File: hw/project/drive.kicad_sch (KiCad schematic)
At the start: 45 parts, among them Q3 STL110N10F7, Q4 STL110N10F7, Q5 STL110N10F7, Q6 STL110N10F7, Q7 STL110N10F7, Q8 STL110N10F7

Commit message: Update sheet settings
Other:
- company: (none) -> Electrium Mobility
- title: (none) -> ESC 2026 - Drive
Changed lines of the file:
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@@
 	(generator_version "10.0")
 	(paper "A4")
+	(title_block
+		(title "ESC 2026 - Drive")
+		(date "2026-06-30")
+		(rev "v2")
+		(company "Electrium Mobility")
+		(comment 1 "Author: Leopoldo Mendoza")
+	)
 	(rectangle
 		(start 93.98 110.49)

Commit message: Continue phase voltage circuit tom
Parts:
- added R52: R_US, Resistor_SMD:R_0805_2012Metric_Pad1.20x1.40mm_HandSolder, symbol Device:R_US
- added R70: R_US, symbol Device:R_US
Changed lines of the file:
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@@
 		)
 	)
+	(text_box "Phase Voltage Sense\n\nExpecting 60Vmax, so R1=47k (0805), R2=2.49k (0603), Cf=2.2nF (>=16V)\n\nNote: Phase Voltage =/= BEMF\n\nBoth FOC and 6-step require the phase voltages to be measured to determine BEMF, thus they require the same circuitry for measuring the phase voltages\n\n6-step\n- With 6-step, zero-crossings are detected EITHER in-software (by sampling the voltage directly with ADC) OR in-hardware (by using a comparator to detect the crossing)\n- This board will only support SOFTWARE-based zero-crossing detection, so the associated pins only require ADCx and not COMPx\n- Note: Virtual Neutral Point could also be determined in either SW or HW, but choosing SW (see Control sheet)"
+		(exclude_from_sim no)
+		(at 78.74 155.194 0)
+		(size 86.36 36.6624)
+		(margins 0.9525 0.9525 0.9525 0.9525)
+		(stroke
+			(width 0)
+			(type solid)
+		)
+		(fill
+			(type none)
+		)
+		(effects
+			(font
+				(size 1.27 1.27)
+			)
+			(justify left top)
+		)
+	)
 	(text_box "PGA Configuration: Inverting Mode (non-inverting disallows DC bias) (AN5306 3.4.1)\n\nVINP (OPP/non-inverting)\n- HW: NC, free up pins with OPAMPx_VINP for other periphs\n- FW: VP_SEL[1:0] = 11 to cut off VINP and route internal DAC ch (RM0440 25.3.4)\n\nVINM (OPN/inverting)\n- HW: small R to limit curr (R1_internal=10k => G_error=0.1%)\n- FW: VM_SEL[1:0] = 10 to enable PGA mode (internal feedback R's) (AN5306 3.4.1)\n\nVOUT (OPO)\n- HW: NC, free up pins with OPAMPx_VOUT for other periphs\n- FW: OPAINTOEN = 1 to cut off VOUT and route internal ADC ch (RM0440 25.3.4)\n\nPGA_GAIN[4:0] = 8 to 13 to implement an inverting amplifier (12=>-31, 13=>-63)"
 		(exclude_from_sim no)
@@
 		)
 	)
+	(label "W"
+		(at 195.58 62.23 0)
+		(effects
+			(font
+				(size 1.27 1.27)
+			)
+			(justify left bottom)
+		)
+	)
 	(label "VSHUNT_U+"
 		(at 38.1 88.9 0)
@@
 		)
 	)
+	(label "U"
+		(at 58.42 60.96 0)
+		(effects
+			(font
+				(size 1.27 1.27)
+			)
+			(justify left bottom)
+		)
+	)
 	(label "VSHUNT_W-"
 		(at 200.66 95.25 0)
@@
 		)
 	)
+	(label "V"
+		(at 127 62.23 0)
+		(effects
+			(font
+				(size 1.27 1.27)
+			)
+			(justify left bottom)
+		)
+	)
 	(label "VSHUNT_V+"
 		(at 92.71 123.19 180)
@@
 		)
 	)
+	(label "U"
+		(at 21.59 158.75 180)
+		(effects
+			(font
+				(size 1.27 1.27)
+			)
+			(justify right bottom)
+		)
+	)
 	(label "VSHUNT_U-"
 		(at 63.5 93.98 0)
@@
 		)
 	)
+	(hierarchical_label "VPHASE_U"
+		(shape output)
+		(at 49.53 157.48 0)
+		(effects
+			(font
+				(size 1.27 1.27)
+			)
+			(justify left)
+		)
+	)
 	(hierarchical_label "GLS3"
 		(shape input)
@@
 	)
 	(symbol
+		(lib_id "Device:R_US")
+		(at 31.75 168.91 180)
+		(unit 1)
+		(body_style 1)
+		(exclude_from_sim no)
+		(in_bom yes)
+		(on_board yes)
+		(in_pos_files yes)
+		(dnp no)
+		(fields_autoplaced yes)
+		(property "Reference" "R70"
+			(at 34.29 167.6399 0)
+			(show_name no)
+			(do_not_autoplace no)
+			(effects
+				(font
+					(size 1.27 1.27)
+				)
+				(justify right)
+			)
+		)
+		(property "Value" "R_US"
+			(at 34.29 170.1799 0)
+			(show_name no)
+			(do_not_autoplace no)
+			(effects
+				(font
+					(size 1.27 1.27)
+				)
+				(justify right)
+			)
+		)
+		(property "Footprint" ""
+			(at 30.734 168.656 90)
+			(hide yes)
+			(show_name no)
+			(do_not_autoplace no)
+			(effects
+				(font
+					(size 1.27 1.27)
+				)
+			)
+		)
+		(property "Datasheet" ""
+			(at 31.75 168.91 0)
+			(hide yes)
+			(show_name no)
+			(do_not_autoplace no)
+			(effects
+				(font
+					(size 1.27 1.27)
+				)
+			)
+		)
+		(property "Description" "Resistor, US symbol"
+			(at 31.75 168.91 0)
+			(hide yes)
+			(show_name no)
+			(do_not_autoplace no)
+			(effects
+				(font
+					(size 1.27 1.27)
+				)
+			)
+		)
+		(pin "1"
+		)
+		(pin "2"
+		)
+		(instances
+			(project "esc"
+				(path "/86a17c4d-db96-42a1-af84-d43fe593f4e6/f702d253-729e-40c3-ac6b-420be83d0138"
+					(reference "R70")
+					(unit 1)
+				)
+			)
+		)
+	)
+	(symbol
 		(lib_id "Device:R_Shunt_US")
 		(at 101.6 92.71 0)
@@
 					(unit 1)
 				)
+			)
+		)
+	)
+	(symbol
+		(lib_id "Device:R_US")
+		(at 31.75 158.75 180)
+		(unit 1)
+		(body_style 1)
+		(exclude_from_sim no)
+		(in_bom yes)
+		(on_board yes)
+		(in_pos_files yes)
+		(dnp no)
+		(fields_autoplaced yes)
+		(property "Reference" "R52"
+			(at 34.29 157.4799 0)
+			(show_name no)
+			(do_not_autoplace no)
+			(effects
+				(font
+					(size 1.27 1.27)
+				)
+				(justify right)
+			)
+		)
+		(property "Value" "R_US"
+			(at 34.29 160.0199 0)
+			(show_name no)
+			(do_not_autoplace no)
+			(effects
+				(font
+					(size 1.27 1.27)
+				)
+				(justify right)
+			)
+		)
+		(property "Footprint" "Resistor_SMD:R_0805_2012Metric_Pad1.20x1.40mm_HandSolder"
+			(at 30.734 158.496 90)
+			(hide yes)
+			(show_name no)
+			(do_not_autoplace no)
+			(effects
+				(font
+					(size 1.27 1.27)
+				)
+			)
+		)
+		(property "Datasheet" ""
+			(at 31.75 158.75 0)
+			(hide yes)
+			(show_name no)
+			(do_not_autoplace no)
+			(effects
+				(font
+					(size 1.27 1.27)
+				)
+			)
+		)
+		(property "Description" "Resistor, US symbol"
+			(at 31.75 158.75 0)
+			(hide yes)
+			(show_name no)
+			(do_not_autoplace no)
+			(effects
+				(font
+					(size 1.27 1.27)
+				)
+			)
+		)
+		(pin "1"
+		)
+		(pin "2"
+		)
+		(instances
+			(project "esc"
+				(path "/86a17c4d-db96-42a1-af84-d43fe593f4e6/f702d253-729e-40c3-ac6b-420be83d0138"
+					(reference "R52")
+					(unit 1)
+				)

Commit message: Add phase voltage first draft
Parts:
- added C23, C52, C54: 470pF/50V, symbol Device:C
- added R72, R76, R79: 2.2k, Resistor_SMD:R_0603_1608Metric_Pad0.98x0.95mm_HandSolder, symbol Device:R_US
- added R74, R75, R77, R78: 22k, Resistor_SMD:R_0603_1608Metric_Pad0.98x0.95mm_HandSolder, symbol Device:R_US
- R52: value R_US -> 22k; footprint Resistor_SMD:R_0805_2012Metric_Pad1.20x1.40mm_HandSolder -> Resistor_SMD:R_0603_1608Metric_Pad0.98x0.95mm_HandSolder
- R70: value R_US -> 22k; footprint (none) -> Resistor_SMD:R_0603_1608Metric_Pad0.98x0.95mm_HandSolder
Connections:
- net GND: now also C23.2, C52.2, C54.2, R72.1, R76.1, R79.1
- net U: now also R70.1
- net V: now also R74.1
- net VPHASE_U: now also R52.2, C23.1, R72.2
- net W: now also R77.1
- net at R70.2: now also R52.1
- new net: R77.2, R78.1
- new net: R74.2, R75.1
- new net VPHASE_V: C52.1, R75.2, R76.2
- new net VPHASE_W: C54.1, R78.2, R79.2
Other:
- note added: "R2/(R1+R2) = 1/21 = 0.04762 {60} [V] -> {2.857} [V]"
- note added: "R_eq = R1 || R2 = 2.1k, C_f = 470 pF => tau = 0.985 us, f_c = 161.6 kHz"
- note added: "Voltage Sense U"
- note added: "Voltage Sense V"
- note added: "Voltage Sense W"
- note added: "add schottkys?"
- note added: "footprint for C_f: C0G (NP0)/5%"
- moved on the sheet: C35, C36, C37, C38, C39, C40, D4, D5, D6, D7, Q5, Q6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

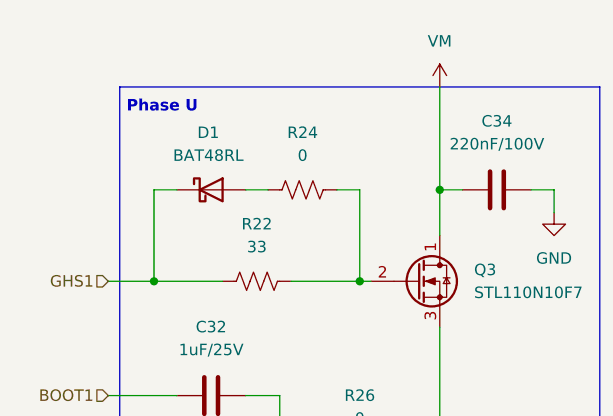
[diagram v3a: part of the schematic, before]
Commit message: Finalize VCC regulator and VDD sections
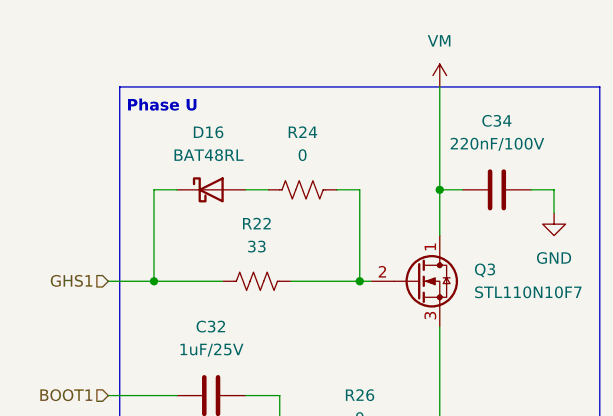
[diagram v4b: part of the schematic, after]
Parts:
- renumbered D1 to D16
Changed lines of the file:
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@@
 		(dnp no)
 		(fields_autoplaced yes)
-		(property "Reference" "D1"
+		(property "Reference" "D16"
 			(at 32.7025 25.4 0)
 			(show_name no)
@@
 			(project "esc"
 				(path "/86a17c4d-db96-42a1-af84-d43fe593f4e6/f702d253-729e-40c3-ac6b-420be83d0138"
-					(reference "D1")
+					(reference "D16")
 					(unit 1)
 				)

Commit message: Finalize phase voltage sensing
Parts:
- removed C33: DNP, symbol Device:C
- removed C39: DNP, Capacitor_SMD:C_0603_1608Metric, symbol Device:C_Small
- removed C52, C54: 470pF/50V, symbol Device:C
- removed R52, R70, R74, R75, R77, R78: 22k, Resistor_SMD:R_0603_1608Metric_Pad0.98x0.95mm_HandSolder, symbol Device:R_US
- removed R76, R79: 2.2k, Resistor_SMD:R_0603_1608Metric_Pad0.98x0.95mm_HandSolder, symbol Device:R_US
- added C33: 470pF/50V, Capacitor_SMD:C_0603_1608Metric, symbol Device:C_Small
- added C57, C58, C59: 1nF, Capacitor_SMD:C_0603_1608Metric, symbol Device:C_Small
- added D35, D36, D37, D38, D39, D40: BAT30K, Diode_SMD:D_SOD-523, symbol Device:D_Schottky
- added R52, R7, R70, R74, R76, R77: 22k, Resistor_SMD:R_0603_1608Metric, symbol Device:R_Small_US
- added R75, R78: 2.2k, Resistor_SMD:R_0603_1608Metric, symbol Device:R_Small_US
- C23: footprint (none) -> Capacitor_SMD:C_0603_1608Metric; symbol Device:C -> Device:C_Small
- C32, C34: symbol Device:C -> Device:C_Small
- C36: value DNP -> 470pF/50V
- R21, R22, R23, R24, R25, R26: symbol Device:R_US -> Device:R_Small_US
- R72: footprint Resistor_SMD:R_0603_1608Metric_Pad0.98x0.95mm_HandSolder -> Resistor_SMD:R_0603_1608Metric; symbol Device:R_US -> Device:R_Small_US
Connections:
- net BOOT1: no longer C32.1
- net GHS1: no longer R22.1
- net GLS1: no longer R23.1
- net GND: now also C33.2, C57.1, C58.1, C59.1, D36.2 (A), D38.2 (A), D40.2 (A), R75.1, R78.1; no longer C34.2
- net OPN_U: now also C57.2; no longer R21.2
- net OPN_V: now also C58.2; no longer C36.1
- net OPN_W: now also C59.2
- net OUT1: no longer C32.2, R26.1
- net U: now also R7.1; no longer R26.2
- net V: now also R70.1
- net VM: no longer C34.1
- net VPHASE_U: now also D35.2 (A), D36.1 (K), R52.2
- net VPHASE_V: now also C33.1, D37.2 (A), D38.1 (K), R74.2, R75.2
- net VPHASE_W: now also C36.1, D39.2 (A), D40.1 (K), R77.2, R78.2
- net VSHUNT_U+: no longer R21.1
- net W: now also R76.1
- net at D3.2 (A): no longer R25.1
- net at R24.1: no longer D16.2 (A)
- new net: R76.2, R77.1
- new net: R70.2, R74.1
- new net: R52.1, R7.2
- new net VDD: D35.1 (K), D37.1 (K), D39.1 (K)
- now unconnected: Q3.2 (G), Q4.2 (G), R22.2, R23.2, R24.2, R25.2
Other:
- note added: "Layout Note: Low-Impedance Power-to-Analog Ground Planes: Ensure your PCB layout uses a continuous, low-impedance ground plane underneath the SoC and power stage. Keep the distance between the low-side shunt ground return and the STSPIN32G4 ground pins as short and wide as possible to minimize $I \times R$ trace resistance and parasitic inductance ($L \times di/dt$). Keep High-Current Paths Away: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"
- note added: "PGND?"
- note removed: "add schottkys?"
- note removed: "footprint for C_f: C0G (NP0)/5%"
- moved on the sheet: C23, R29, R37

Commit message: Work on rest of drive tomorrow
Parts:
- removed R21: 10, symbol Device:R_Small_US
- added R79: 10, Resistor_SMD:R_0603_1608Metric, symbol Device:R_Small_US
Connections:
- net OPN_U: now also R79.2
- net VSHUNT_U+: now also R79.1
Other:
- note added: "C0G/NP0 required!! so cant reuse hall sensor's 1nF, but can just it for all"
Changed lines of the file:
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@@
 	(generator "eeschema")
 	(generator_version "10.0")
-	(paper "A3")
+	(paper "User" 330.2 228.6)
 	(title_block
 		(title "ESC 2026 - Drive")
@@
 		)
 	)
+	(text "C0G/NP0 required!!\n\nso cant reuse hall sensor's 1nF, but can just it for all"
+		(exclude_from_sim no)
+		(at 93.726 131.064 0)
+		(effects
+			(font
+				(size 1.27 1.27)
+				(color 255 4 4 1)
+			)
+			(justify left)
+		)
+	)
 	(text "Voltage Sense U"
 		(exclude_from_sim no)
@@
 	(text_box "Bootstrap Cap (BOOTx - OUTx)\n\nFor STL110N10F7, since V_GS(th, max) = 4.5V and R_DS(on, max) spec'd at V_GS = 10V, VCC = 10V set in FW\n\nC_BOOT(min) >= (10*Q_g)/V_GS = (10*72nC)/10V = 72nF\n\nBut take 1uF from EVSPIN32G4 for plenty of safety buffer against voltage sag while remaining small enough to fully recharge when GLSx on"
 		(exclude_from_sim no)
-		(at 223.52 40.64 0)
-		(size 86.36 20.3053)
+		(at 223.52 38.1 0)
+		(size 86.36 22.8453)
 		(margins 0.9525 0.9525 0.9525 0.9525)
 		(stroke
@@
 		(exclude_from_sim no)
 		(at 223.52 20.32 0)
-		(size 86.36 15.2399)
+		(size 86.36 17.7799)
 		(margins 0.9525 0.9525 0.9525 0.9525)
 		(stroke
@@
 		)
 	)
-	(text_box "External Filtering Resistor: R_f = 10 ohms\nInternal op-amp has high input impedance, so effect on measurement is negligible\n\nExternal Filtering Capacitor: C_f = 1 nF\nSTM32G431C6 datasheet gives GBW_min=7MHz & BW_PGA=GBW/G, so G_worst=-63 => BW_worst=7MHz/64=109kHz > f_FOC=50kHz\nTheoretically fine to DNP a C_f, but add 1nF anyway to prevent high-freq MOSFET switching noise before captured by the ADC\nC_f cannot hurt since f_c=15.91MHz >>> 109kHz=BW_worst"
+	(text_box "External Filtering Resistor: R_f = 10 ohms\nInternal op-amp has high input impedance, so effect on measurement is negligible\n\nExternal Filtering Capacitor: C_f = 1 nF (C0G/NP0 is a MUST)\nSTM32G431C6 datasheet gives GBW_min=7MHz & BW_PGA=GBW/G, so G_worst=-63 => BW_worst=7MHz/64=109kHz > f_FOC=50kHz\nTheoretically fine to DNP a C_f, but add 1nF anyway to prevent high-freq MOSFET switching noise before captured by the ADC\nC_f cannot hurt since f_c=15.91MHz >>> 109kHz=BW_worst"
 		(exclude_from_sim no)
 		(at 241.3 119.38 0)
@@
 	(wire
 		(pts
-			(xy 36.83 121.92) (xy 39.37 121.92)
-		)
-		(stroke
-			(width 0)
-			(type default)
-		)
-	)
-	(wire
-		(pts
 			(xy 97.79 69.85) (xy 95.25 69.85)
 		)
@@
 	(wire
 		(pts
+			(xy 35.56 121.92) (xy 39.37 121.92)
+		)
+		(stroke
+			(width 0)
+			(type default)
+		)
+	)
+	(wire
+		(pts
 			(xy 101.6 85.09) (xy 101.6 86.36)
 		)
@@
 	(wire
 		(pts
-			(xy 24.13 121.92) (xy 29.21 121.92)
+			(xy 24.13 121.92) (xy 30.48 121.92)
 		)
 		(stroke
@@
 	)
 	(symbol
-		(lib_id "Device:C_Small")
-		(at 135.89 128.27 180)
+		(lib_id "Device:R_Small_US")
+		(at 33.02 121.92 90)
 		(unit 1)
 		(body_style 1)
@@
 		(in_pos_files yes)
 		(dnp no)
-		(fields_autoplaced yes)
-		(property "Reference" "C59"
-			(at 138.43 126.9935 0)
+		(property "Reference" "R79"
+			(at 33.274 116.078 90)
 			(show_name no)
 			(do_not_autoplace no)
@@
 					(size 1.27 1.27)
 				)
-				(justify right)
 			)
 		)
-		(property "Value" "1nF"
-			(at 138.43 129.5335 0)
+		(property "Value" "10"
+			(at 33.274 118.618 90)
 			(show_name no)
 			(do_not_autoplace no)
@@
 					(size 1.27 1.27)
 				)
-				(justify right)
 			)
 		)
-		(property "Footprint" "Capacitor_SMD:C_0603_1608Metric"
-			(at 135.89 128.27 0)
+		(property "Footprint" "Resistor_SMD:R_0603_1608Metric"
+			(at 33.02 121.92 0)
 			(hide yes)
 			(show_name no)
@@
 			)
 		)
-		(property "Datasheet" ""
-			(at 135.89 128.27 0)
+		(property "Datasheet" "https://www.digikey.ca/en/products/detail/stackpole-electronics-inc/RMCF0603FT10R0/1761152"
+			(at 33.02 121.92 0)
 			(hide yes)
 			(show_name no)
@@
 			)
 		)
-		(property "Description" "Unpolarized capacitor, small symbol"
-			(at 135.89 128.27 0)
+		(property "Description" "RES 10 OHM 1% 1/10W 0603"
+			(at 33.02 121.92 0)
 			(hide yes)
 			(show_name no)
@@
 			)
 		)
-		(pin "2"
-		)
 		(pin "1"
 		)
+		(pin "2"
+		)
 		(instances
 			(project "esc"
 				(path "/86a17c4d-db96-42a1-af84-d43fe593f4e6/f702d253-729e-40c3-ac6b-420be83d0138"
-					(reference "C59")
+					(reference "R79")
 					(unit 1)
 				)
@@
 	(symbol
 		(lib_id "Device:C_Small")
-		(at 180.34 166.37 0)
+		(at 135.89 128.27 180)
 		(unit 1)
 		(body_style 1)
@@
 		(dnp no)
 		(fields_autoplaced yes)
-		(property "Reference" "C36"
-			(at 182.88 165.1062 0)
+		(property "Reference" "C59"
+			(at 138.43 126.9935 0)
 			(show_name no)
 			(do_not_autoplace no)
@@
 					(size 1.27 1.27)
 				)
-				(justify left)
+				(justify right)
 			)
 		)
-		(property "Value" "470pF/50V"
-			(at 182.88 167.6462 0)
+		(property "Value" "1nF"
+			(at 138.43 129.5335 0)
 			(show_name no)
 			(do_not_autoplace no)
@@
 					(size 1.27 1.27)
 				)
-				(justify left)
+				(justify right)
 			)
 		)
 		(property "Footprint" "Capacitor_SMD:C_0603_1608Metric"
-			(at 180.34 166.37 0)
+			(at 135.89 128.27 0)
 			(hide yes)
 			(show_name no)
@@
 			)
 		)
-		(property "Datasheet" "https://www.digikey.ca/en/products/detail/vishay-vitramon/VJ0603A471FXACW1BC/8304296"
-			(at 180.34 166.37 0)
+		(property "Datasheet" ""
+			(at 135.89 128.27 0)
 			(hide yes)
 			(show_name no)
@@
 			)
 		)
-		(property "Description" "CAP CER 470PF 50V C0G/NP0 0603"
-			(at 180.34 166.37 0)
+		(property "Description" "Unpolarized capacitor, small symbol"
+			(at 135.89 128.27 0)
 			(hide yes)
 			(show_name no)
@@
 			(project "esc"
 				(path "/86a17c4d-db96-42a1-af84-d43fe593f4e6/f702d253-729e-40c3-ac6b-420be83d0138"
-					(reference "C36")
+					(reference "C59")
 					(unit 1)
 				)
@@
 	)
 	(symbol
-		(lib_id "Device:R_Small_US")
-		(at 118.11 60.96 90)
+		(lib_id "Device:C_Small")
+		(at 180.34 166.37 0)
 		(unit 1)
 		(body_style 1)
@@
 		(in_pos_files yes)
 		(dnp no)
-		(property "Reference" "R34"
-			(at 118.364 55.118 90)
+		(fields_autoplaced yes)
+		(property "Reference" "C36"
+			(at 182.88 165.1062 0)
 			(show_name no)
 			(do_not_autoplace no)
@@
 					(size 1.27 1.27)
 				)
+				(justify left)
 			)
 		)
-		(property "Value" "0"
-			(at 118.364 57.658 90)
+		(property "Value" "470pF/50V"
+			(at 182.88 167.6462 0)
 			(show_name no)
 			(do_not_autoplace no)
@@
 					(size 1.27 1.27)
 				)
+				(justify left)
 			)
 		)
-		(property "Footprint" "Resistor_SMD:R_0603_1608Metric"
-			(at 118.11 60.96 0)
+		(property "Footprint" "Capacitor_SMD:C_0603_1608Metric"
+			(at 180.34 166.37 0)
 			(hide yes)
 			(show_name no)
@@
 			)
 		)
-		(property "Datasheet" "https://www.digikey.ca/en/products/detail/stackpole-electronics-inc/RMCF0603ZT0R00/1756908"
-			(at 118.11 60.96 0)
+		(property "Datasheet" "https://www.digikey.ca/en/products/detail/vishay-vitramon/VJ0603A471FXACW1BC/8304296"
+			(at 180.34 166.37 0)
 			(hide yes)
 			(show_name no)
@@
 			)
 		)
-		(property "Description" "RES 0 OHM JUMPER 1/10W 0603"
-			(at 118.11 60.96 0)
+		(property "Description" "CAP CER 470PF 50V C0G/NP0 0603"
+			(at 180.34 166.37 0)
 			(hide yes)
 			(show_name no)
@@
 			)
 		)
-		(pin "1"
-		)
 		(pin "2"
 		)
+		(pin "1"
+		)
 		(instances
 			(project "esc"
 				(path "/86a17c4d-db96-42a1-af84-d43fe593f4e6/f702d253-729e-40c3-ac6b-420be83d0138"
-					(reference "R34")
+					(reference "C36")
 					(unit 1)
 				)
@@
 	(symbol
 		(lib_id "Device:R_Small_US")
-		(at 33.02 121.92 90)
+		(at 118.11 60.96 90)
 		(unit 1)
 		(body_style 1)
@@
 		(in_pos_files yes)
 		(dnp no)
-		(fields_autoplaced yes)
-		(property "Reference" "R21"
-			(at 33.02 115.57 90)
+		(property "Reference" "R34"
+			(at 118.364 55.118 90)
 			(show_name no)
 			(do_not_autoplace no)
@@
 			)
 		)
-		(property "Value" "10"
-			(at 33.02 118.11 90)
+		(property "Value" "0"
+			(at 118.364 57.658 90)
 			(show_name no)
 			(do_not_autoplace no)
@@
 			)
 		)
-		(property "Footprint" ""
-			(at 33.02 121.92 0)
+		(property "Footprint" "Resistor_SMD:R_0603_1608Metric"
+			(at 118.11 60.96 0)
 			(hide yes)
 			(show_name no)
@@
 			)
 		)
-		(property "Datasheet" ""
-			(at 33.02 121.92 0)
+		(property "Datasheet" "https://www.digikey.ca/en/products/detail/stackpole-electronics-inc/RMCF0603ZT0R00/1756908"
+			(at 118.11 60.96 0)
 			(hide yes)
 			(show_name no)
@@
 			)
 		)
-		(property "Description" "Resistor, small US symbol"
-			(at 33.02 121.92 0)
+		(property "Description" "RES 0 OHM JUMPER 1/10W 0603"
+			(at 118.11 60.96 0)
 			(hide yes)
 			(show_name no)
@@
 			)
 		)
-		(pin "2"
-		)
 		(pin "1"
 		)
+		(pin "2"
+		)
 		(instances
 			(project "esc"
 				(path "/86a17c4d-db96-42a1-af84-d43fe593f4e6/f702d253-729e-40c3-ac6b-420be83d0138"
-					(reference "R21")
+					(reference "R34")
 					(unit 1)
 				)
